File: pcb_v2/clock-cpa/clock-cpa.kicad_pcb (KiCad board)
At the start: 2 copper layers, 121.9 x 33 mm, 30 parts, among them J1 clock_ext, J2 control panel, J3 control panel, SW1 1HZ, SW2 1KHZ, SW3 XTAL1, SW4 XTAL2, SW5 EXT, SW6 BREAK, SW7 CLOCK_RESET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

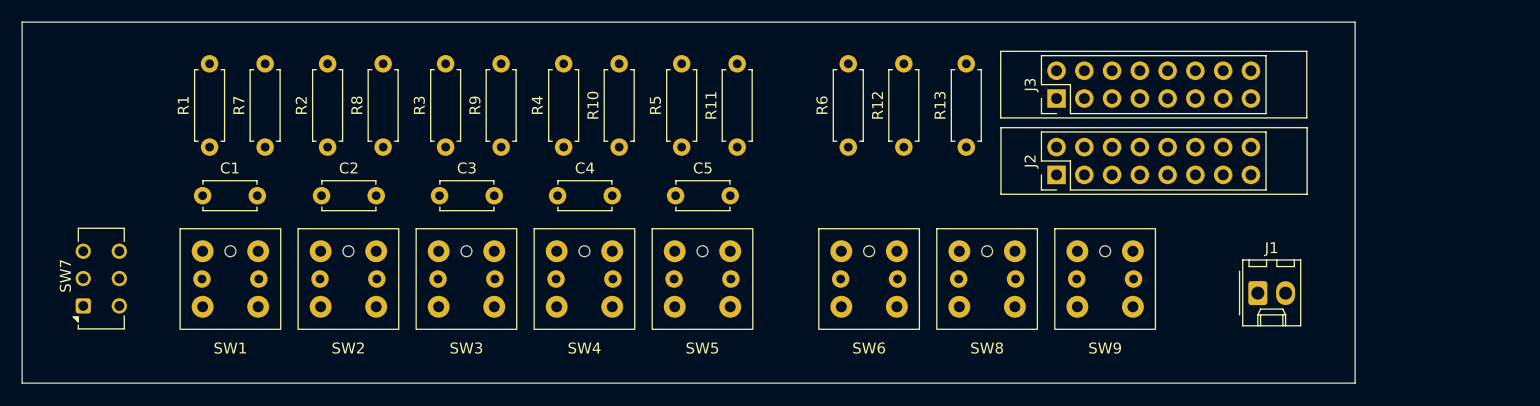
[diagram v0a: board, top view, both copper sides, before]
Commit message: layout do painel de controle do gerador de clock
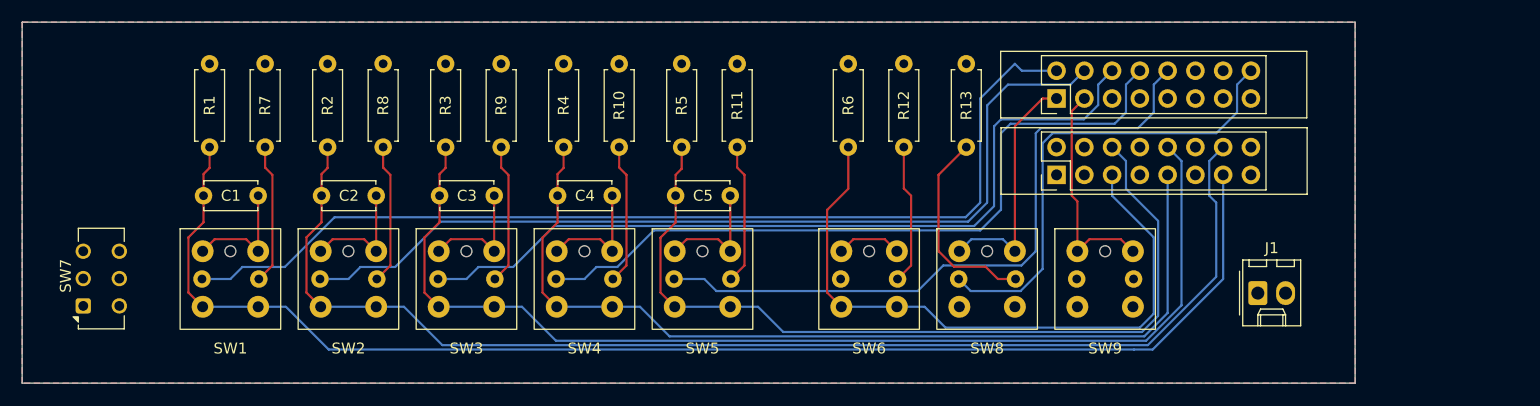
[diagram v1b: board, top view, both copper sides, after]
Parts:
- moved C1 5.08 mm to (65.4, 76.8), turned to 180 degrees
- moved C2 5.00 mm to (76.2, 76.8), turned to 180 degrees
- moved C3 5.00 mm to (87.0, 76.8), turned to 180 degrees
- moved C4 5.00 mm to (97.8, 76.8), turned to 180 degrees
- moved C5 5.00 mm to (108.6, 76.8), turned to 180 degrees
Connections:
- J2 pad 10: xtal2_out -> xtal1_out
- J2 pad 11: 1KHz_in -> 1Hz_in
- J2 pad 12: ext_in -> 1KHz_in
- J2 pad 13: 1KHz_out -> 1Hz_out
- J2 pad 14: ext_out -> 1KHz_out
- J2 pad 4: xtal1_in -> ext_in
- J2 pad 6: xtal1_out -> ext_out
- J2 pad 7: 1Hz_in -> xtal2_in
- J2 pad 8: xtal2_in -> xtal1_in
- J2 pad 9: 1Hz_out -> xtal2_out
- J3 pad 1: step -> half_step
- J3 pad 12: clock_stopped -> ~{clock_stopped}
- J3 pad 3: half_step -> step
- R12 pad 2: GND -> ~{clock_stopped}
- SW6 pad 4: clock_stopped -> +5V
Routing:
- net 1Hz_out: track 0.00 -> 123.1 mm
- net 1KHz_out: track 0.00 -> 114.6 mm
- net xtal1_out: track 0.00 -> 101.5 mm
- net clock_1hz: track 0.00 -> 92.2 mm
- net xtal2_out: track 0.00 -> 86.5 mm
- net clock_1Khz: track 0.00 -> 83.0 mm
- net ext_out: track 0.00 -> 78.9 mm
- net clock_xtal1: track 0.00 -> 74.9 mm
- net clock_xtal2: track 0.00 -> 66.9 mm
- net clock_ext: track 0.00 -> 61.8 mm
- net break_out: track 0.00 -> 60.1 mm
- net clock_pulse: track 0.00 -> 43.8 mm
- net half_step: track 0.00 -> 22.3 mm
- net step: track 0.00 -> 20.7 mm
- net Net-(SW8-K): track 0.00 -> 18.7 mm
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- added copper zone on B.Cu, net GND
- added copper zone on F.Cu, net GND

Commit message: Adicionado a porta para clock out; trabalhando no roteamento
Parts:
- added J4: CLK OUT, Connector_Molex:Molex_KK-254_AE-6410-02A_1x02_P2.54mm_Vertical, F.Cu at (165.1, 85.7)
- J1: value clock_ext -> EXT IN
- moved J2 8.19 mm to (146.6, 74.9)
- moved J3 8.19 mm to (146.6, 67.9)
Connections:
- J2 pad 10: xtal1_out -> break_out
- J2 pad 11: 1Hz_in -> xtal1_out
- J2 pad 12: 1KHz_in -> xtal2_out
- J2 pad 3: break_in -> 1KHz_in
- J2 pad 4: ext_in -> 1Hz_in
- J2 pad 5: break_out -> xtal2_in
- J2 pad 6: ext_out -> xtal1_in
- J2 pad 7: xtal2_in -> break_in
- J2 pad 8: xtal1_in -> ext_in
- J2 pad 9: xtal2_out -> ext_out
- J3 pad 7: unconnected-(J3-Pin_7-Pad7) -> clock_out
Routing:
- net clock_reset_in: track 0.00 -> 104.2 mm, vias 0 -> 1
- net 1Hz_in: track 11.1 -> 88.5 mm
- net 1KHz_in: track 11.1 -> 78.9 mm
- net xtal1_in: track 11.1 -> 73.2 mm
- net xtal2_in: track 11.1 -> 60.6 mm
- net +5V: track 0.00 -> 44.7 mm, vias 0 -> 1
- net ext_in: track 11.1 -> 52.4 mm
- net xtal1_out: track 101.5 -> 130.2 mm
- net break_in: track 5.99 -> 32.1 mm
- net ~{clock_stopped}: track 0.00 -> 25.3 mm
- net clock_xtal2: track 66.9 -> 58.8 mm, vias 0 -> 2
- net clock_xtal1: track 74.9 -> 67.4 mm, vias 0 -> 2
- net ext_out: track 78.9 -> 72.6 mm
- net 1KHz_out: track 114.6 -> 108.6 mm
- net clock_pulse: track 43.8 -> 37.8 mm, vias 0 -> 2
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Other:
- board size 121.9 x 33 mm -> 127 x 33 mm

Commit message: layout de pcb do clock
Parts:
- added R15: 10K, Resistor_THT:R_Axial_DIN0207_L6.3mm_D2.5mm_P7.62mm_Horizontal, F.Cu at (110.5, 72.4)
- added R21: 10K, Resistor_THT:R_Axial_DIN0207_L6.3mm_D2.5mm_P7.62mm_Horizontal, F.Cu at (130.8, 72.4)
- J1, J4: footprint Connector_Molex:Molex_KK-254_AE-6410-02A_1x02_P2.54mm_Vertical -> Connector_JST:JST_XH_B2B-XH-A_1x02_P2.50mm_Vertical
- moved J1 15.7 mm to (167.6, 74.3), turned to 180 degrees
- moved J2 7.56 mm to (139.1, 74.9)
- moved J3 7.56 mm to (139.1, 67.9)
- moved SW7 6.35 mm to (49.4, 80.6)
- moved J4 4.58 mm to (167.6, 81.9), turned to 180 degrees
- moved R13 4.45 mm to (125.7, 72.4)
- moved R11 3.81 mm to (105.4, 72.4)
- moved R5 3.81 mm to (100.3, 72.4)
- moved R6 3.81 mm to (115.6, 72.4)
- moved R12 3.81 mm to (120.7, 72.4)
- moved R10 3.17 mm to (95.2, 72.4)
- moved R4 3.17 mm to (90.2, 72.4)
- moved R3 2.54 mm to (80.0, 72.4)
- moved R9 2.54 mm to (85.1, 72.4)
- moved R2 1.91 mm to (69.8, 72.4)
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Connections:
- J3 pad 11: unconnected-(J3-Pin_11-Pad11) -> signal_ext
- J3 pad 14: signal_ext -> unconnected-(J3-Pin_14-Pad14)
- J3 pad 16: clock_pulse -> unconnected-(J3-Pin_16-Pad16)
- J3 pad 9: unconnected-(J3-Pin_9-Pad9) -> clock_pulse
- SW7 pad 1: xtal1_out -> unconnected-(SW7-A-Pad1)
- SW7 pad 2: clock_reset_in -> xtal1_out
- SW7 pad 3: unconnected-(SW7-C-Pad3) -> clock_reset_in
- SW7 pad 4: unconnected-(SW7-A-Pad4) -> clock_reset_in
- SW7 pad 5: unconnected-(SW7-B-Pad5) -> xtal1_out
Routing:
- net +5V: track 44.7 -> 81.0 mm
- net clock_out: track 0.00 -> 28.4 mm
- net half_step: track 22.3 -> 49.6 mm, vias 0 -> 2
- net step: track 20.7 -> 44.7 mm, vias 0 -> 1
- net signal_ext: track 0.00 -> 16.0 mm
- net xtal1_out: track 130.2 -> 140.9 mm
- net clock_xtal2: track 58.8 -> 69.0 mm, vias 2 -> 1
- net clock_xtal1: track 67.4 -> 76.8 mm, vias 2 -> 1
- net ~{clock_stopped}: track 25.3 -> 33.2 mm
- net 1KHz_out: track 108.6 -> 116.1 mm
- net break_out: track 58.0 -> 65.2 mm
- net xtal2_out: track 86.0 -> 92.7 mm
- net ext_out: track 72.6 -> 78.2 mm
- net clock_reset_in: track 104.2 -> 98.6 mm, vias 1 -> 0
- net clock_1Khz: track 78.3 -> 83.8 mm, vias 2 -> 1
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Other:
- board size 127 x 33 mm -> 129.5 x 33 mm
- board text added: "AUTO"
- board text added: "CLOCK GEN"
- board text added: "GND"
- board text added: "MANUAL"
- board text added: "SIGNAL"

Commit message: continuando implementação do clock
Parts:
- removed C4: 100nF, Capacitor_THT:C_Disc_D4.7mm_W2.5mm_P5.00mm
- removed R10: 1K, Resistor_THT:R_Axial_DIN0207_L6.3mm_D2.5mm_P7.62mm_Horizontal
- removed R4: 10K, Resistor_THT:R_Axial_DIN0207_L6.3mm_D2.5mm_P7.62mm_Horizontal
- removed SW4: XTAL2, clock-buttons:TS5 LED Momentary Click Tact Switch
- SW3: value XTAL1 -> XTAL
- SW7: footprint Button_Switch_THT:SW_CK_JS202011CQN_DPDT_Straight -> clock-buttons:Slide Switch DPDT
- moved SW7 113.8 mm to (163.2, 77.5), turned to 0 degrees
- moved J4 26.4 mm to (141.6, 86.4), turned to 90 degrees
- moved J1 22.0 mm to (149.2, 86.3), turned to 90 degrees
- moved J2 11.4 mm to (127.6, 74.9)
- moved J3 11.4 mm to (127.6, 67.9)
- moved SW8 10.8 mm to (121.3, 84.5)
- moved SW5 10.8 mm to (95.2, 84.5)
- moved SW6 10.8 mm to (110.5, 84.5)
- moved C5 10.8 mm to (97.8, 76.8)
- moved SW9 10.8 mm to (132.1, 84.5)
- moved R12 10.2 mm to (110.5, 72.4)
- moved R13 10.2 mm to (115.6, 72.4)
- moved R11 10.2 mm to (95.2, 72.4)
- moved R15 10.2 mm to (100.3, 72.4)
- moved R21 10.2 mm to (120.7, 72.4)
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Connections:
- J2 pad 12: xtal2_out -> unconnected-(J2-Pin_12-Pad12)
- J2 pad 5: xtal2_in -> unconnected-(J2-Pin_5-Pad5)
- J3 pad 8: clock_xtal2 -> unconnected-(J3-Pin_8-Pad8)
- SW7 pad 1: unconnected-(SW7-A-Pad1) -> clock_reset_in
- SW7 pad 3: clock_reset_in -> unconnected-(SW7-C-Pad3)
- SW7 pad 4: clock_reset_in -> unconnected-(SW7-A-Pad4)
- SW7 pad 6: unconnected-(SW7-C-Pad6) -> clock_reset_in
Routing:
- net xtal2_out: track 92.7 -> 0.00 mm
- net clock_xtal2: track 69.0 -> 0.00 mm, vias 1 -> 0
- net xtal2_in: track 62.1 -> 0.00 mm
- net clock_reset_in: track 98.6 -> 38.5 mm, vias 0 -> 1
- net xtal1_out: track 140.9 -> 117.6 mm
- net 1KHz_in: track 80.7 -> 66.0 mm
- net xtal1_in: track 74.6 -> 60.2 mm
- net Net-(SW4-K): track 14.2 -> 0.00 mm
- net 1Hz_in: track 91.6 -> 77.8 mm
- net clock_1Khz: track 83.8 -> 70.1 mm
- net step: track 44.7 -> 31.1 mm, vias 1 -> 0
- net clock_1hz: track 91.5 -> 78.2 mm
- net +5V: track 81.0 -> 68.8 mm
- net clock_xtal1: track 76.8 -> 65.1 mm
- net 1Hz_out: track 125.3 -> 114.1 mm
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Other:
- board size 129.5 x 33 mm -> 133.3 x 33 mm
- board text added: "BREAK"
- board text removed: "MANUAL"

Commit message: usando a nova chave de slide, posicionado a direita
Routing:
- net half_step: track 47.2 -> 53.9 mm, vias 1 -> 0
- net clock_out: track 22.2 -> 20.2 mm
- net clock_ext: track 59.0 -> 57.9 mm
- net ~{clock_stopped}: track 31.5 -> 32.2 mm
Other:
- board text added: "A"
- board text added: "B"

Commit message: layout de pcb pronto para fabricação
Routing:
- net half_step: track 53.9 -> 52.4 mm
- net xtal1_out: track 117.6 -> 116.5 mm, vias 0 -> 1
- net clock_reset_in: track 38.5 -> 39.6 mm, vias 1 -> 2
- net Net-(SW3-K): track 13.9 -> 12.9 mm
- net Net-(SW5-K): track 14.2 -> 13.1 mm
- net Net-(SW6-K): track 14.2 -> 13.1 mm
- net Net-(SW2-K): track 13.6 -> 12.6 mm
- net 1Hz_out: track 114.1 -> 113.5 mm

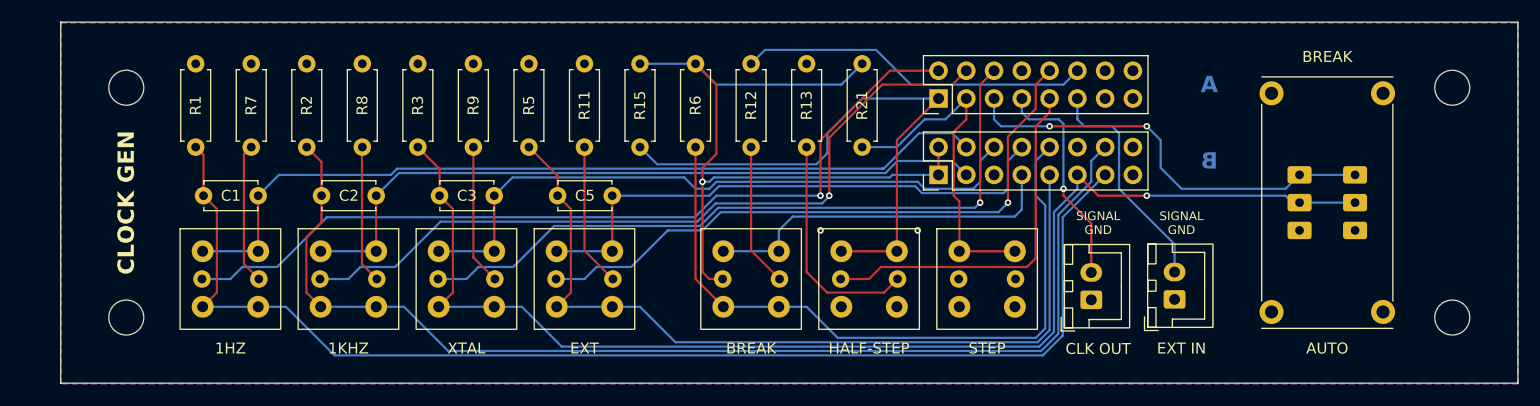
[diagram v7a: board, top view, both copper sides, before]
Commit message: tamanho dos conectores estava errado
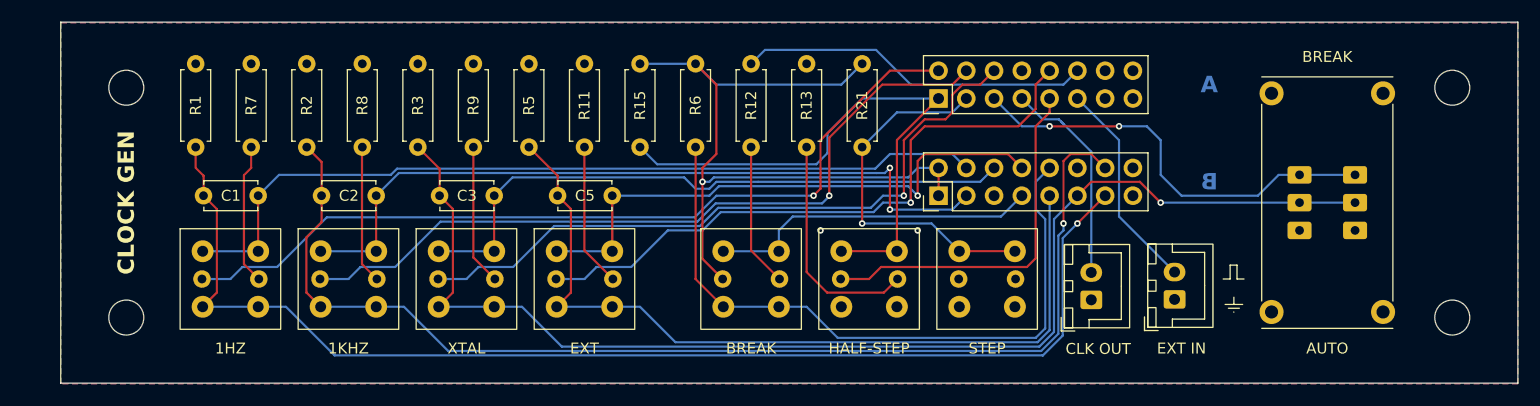
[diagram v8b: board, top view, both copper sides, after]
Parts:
- moved J2 1.90 mm to (127.6, 76.8)
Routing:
- net 1KHz_in: track 66.0 -> 69.5 mm, vias 0 -> 2
- net break_in: track 33.2 -> 30.5 mm
- net xtal1_in: track 60.2 -> 57.8 mm
- net clock_xtal1: track 65.1 -> 62.7 mm
- net step: track 31.1 -> 33.4 mm, vias 0 -> 1
- net 1Hz_out: track 113.5 -> 111.6 mm, vias 0 -> 1
- net ext_out: track 77.8 -> 75.9 mm
- net break_out: track 64.1 -> 62.2 mm
- net 1KHz_out: track 104.9 -> 106.7 mm, vias 0 -> 1
- net xtal1_out: track 116.5 -> 114.9 mm
- net signal_ext: track 21.0 -> 19.6 mm
- net ext_in: track 51.5 -> 52.3 mm, vias 0 -> 1
- net 1Hz_in: track 77.8 -> 77.0 mm
- net clock_out: track 20.2 -> 19.7 mm, vias 1 -> 0
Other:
- board text removed: "GND"
- board text removed: "SIGNAL"
